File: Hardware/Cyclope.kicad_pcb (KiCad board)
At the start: 2 copper layers, 71 parts, among them J1 M20-9762042, J2 Motor_2, J3 Motor_1, J4 Camera_Right, J5 Camera_Left, J6 Motherboard_Right, J7 Motherboard_Left, J8 FTDI, M1 FS5113R, M2 FS5113R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

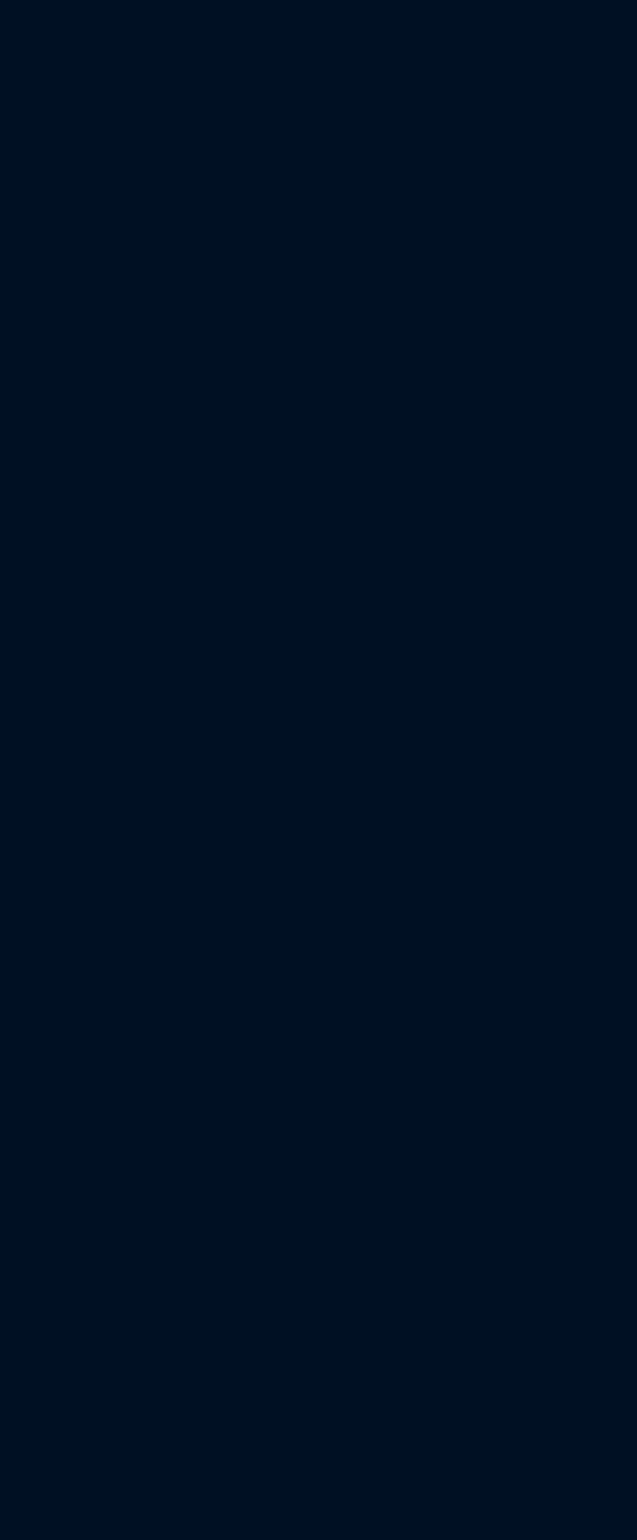
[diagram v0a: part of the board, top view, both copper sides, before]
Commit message: [Hardware] Added front board dimensions to PCB.
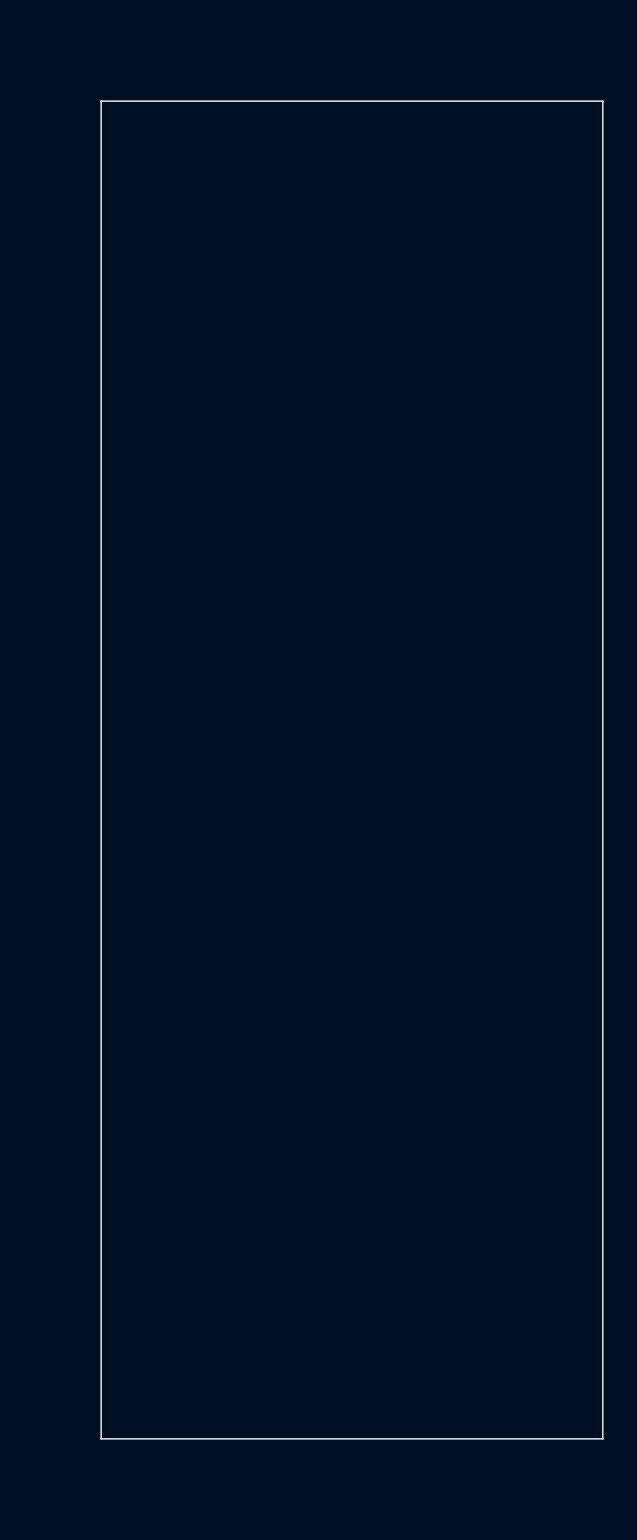
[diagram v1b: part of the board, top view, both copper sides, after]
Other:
- board outline added: 30 x 80 mm
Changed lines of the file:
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@@
   (general
     (thickness 1.6)
-    (drawings 1)
+    (drawings 8)
     (tracks 0)
     (zones 0)
@@
     )
   )
+  (dimension 25 (width 0.15) (layer Dwgs.User)
+    (gr_text "25,000 mm" (at 252.3 79.5 270) (layer Dwgs.User)
+      (effects (font (size 1 1) (thickness 0.15)))
+    )
+    (feature1 (pts (xy 240 92) (xy 251.586421 92)))
+    (feature2 (pts (xy 240 67) (xy 251.586421 67)))
+    (crossbar (pts (xy 251 67) (xy 251 92)))
+    (arrow1a (pts (xy 251 92) (xy 250.413579 90.873496)))
+    (arrow1b (pts (xy 251 92) (xy 251.586421 90.873496)))
+    (arrow2a (pts (xy 251 67) (xy 250.413579 68.126504)))
+    (arrow2b (pts (xy 251 67) (xy 251.586421 68.126504)))
+  )
+  (dimension 16 (width 0.15) (layer Dwgs.User)
+    (gr_text "16,000 mm" (at 252.3 48 270) (layer Dwgs.User)
+      (effects (font (size 1 1) (thickness 0.15)))
+    )
+    (feature1 (pts (xy 240 56) (xy 251.586421 56)))
+    (feature2 (pts (xy 240 40) (xy 251.586421 40)))
+    (crossbar (pts (xy 251 40) (xy 251 56)))
+    (arrow1a (pts (xy 251 56) (xy 250.413579 54.873496)))
+    (arrow1b (pts (xy 251 56) (xy 251.586421 54.873496)))
+    (arrow2a (pts (xy 251 40) (xy 250.413579 41.126504)))
+    (arrow2b (pts (xy 251 40) (xy 251.586421 41.126504)))
+  )
+  (dimension 16 (width 0.15) (layer Dwgs.User)
+    (gr_text "16,000 mm" (at 254.3 112 90) (layer Dwgs.User)
+      (effects (font (size 1 1) (thickness 0.15)))
+    )
+    (feature1 (pts (xy 240 104) (xy 253.586421 104)))
+    (feature2 (pts (xy 240 120) (xy 253.586421 120)))
+    (crossbar (pts (xy 253 120) (xy 253 104)))
+    (arrow1a (pts (xy 253 104) (xy 253.586421 105.126504)))
+    (arrow1b (pts (xy 253 104) (xy 252.413579 105.126504)))
+    (arrow2a (pts (xy 253 120) (xy 253.586421 118.873496)))
+    (arrow2b (pts (xy 253 120) (xy 252.413579 118.873496)))
+  )
+  (gr_line (start 240 40) (end 240 120) (layer Edge.Cuts) (width 0.1))
+  (gr_line (start 210 40) (end 240 40) (layer Edge.Cuts) (width 0.1))
+  (gr_line (start 210 120) (end 210 40) (layer Edge.Cuts) (width 0.1))
+  (gr_line (start 240 120) (end 210 120) (layer Edge.Cuts) (width 0.1))
   (gr_text GND (at 169.164 113.792) (layer F.Mask)
     (effects (font (size 1 1) (thickness 0.15)))

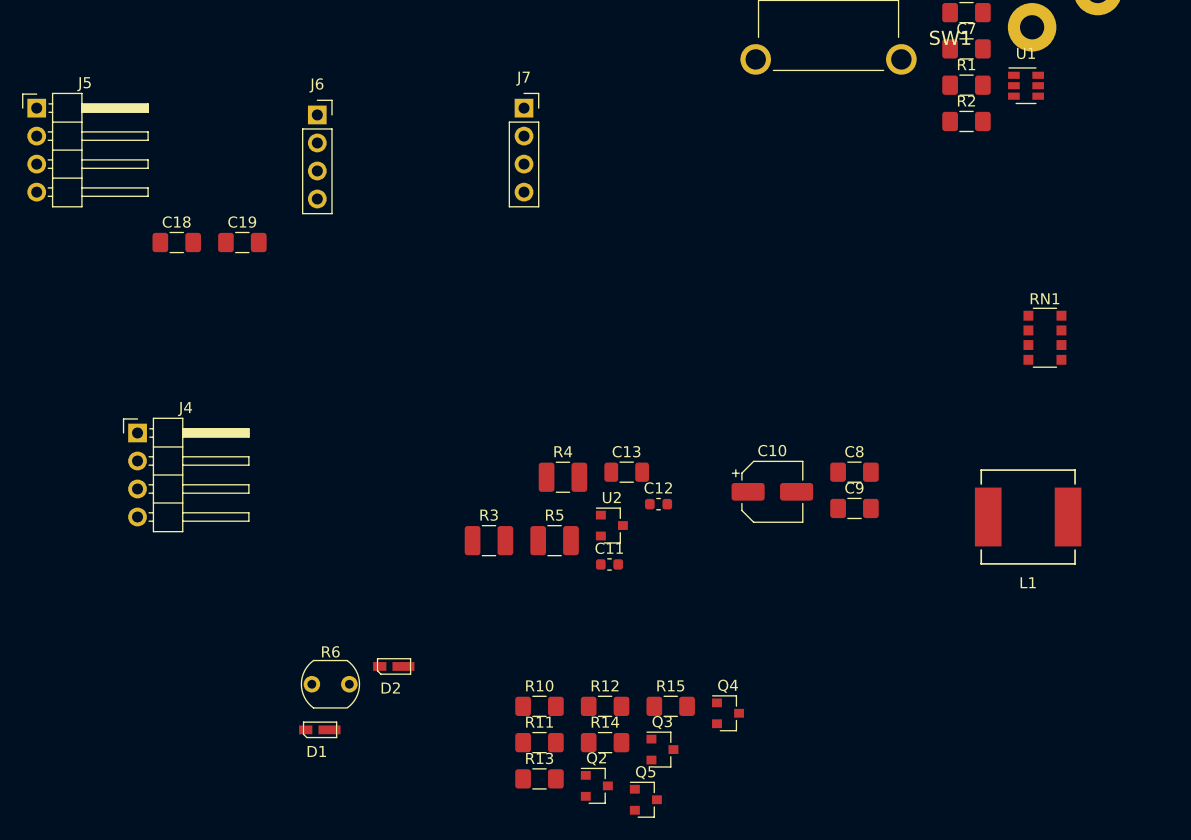
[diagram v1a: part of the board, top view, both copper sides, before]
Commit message: [Hardware] Added front board mounting holes.
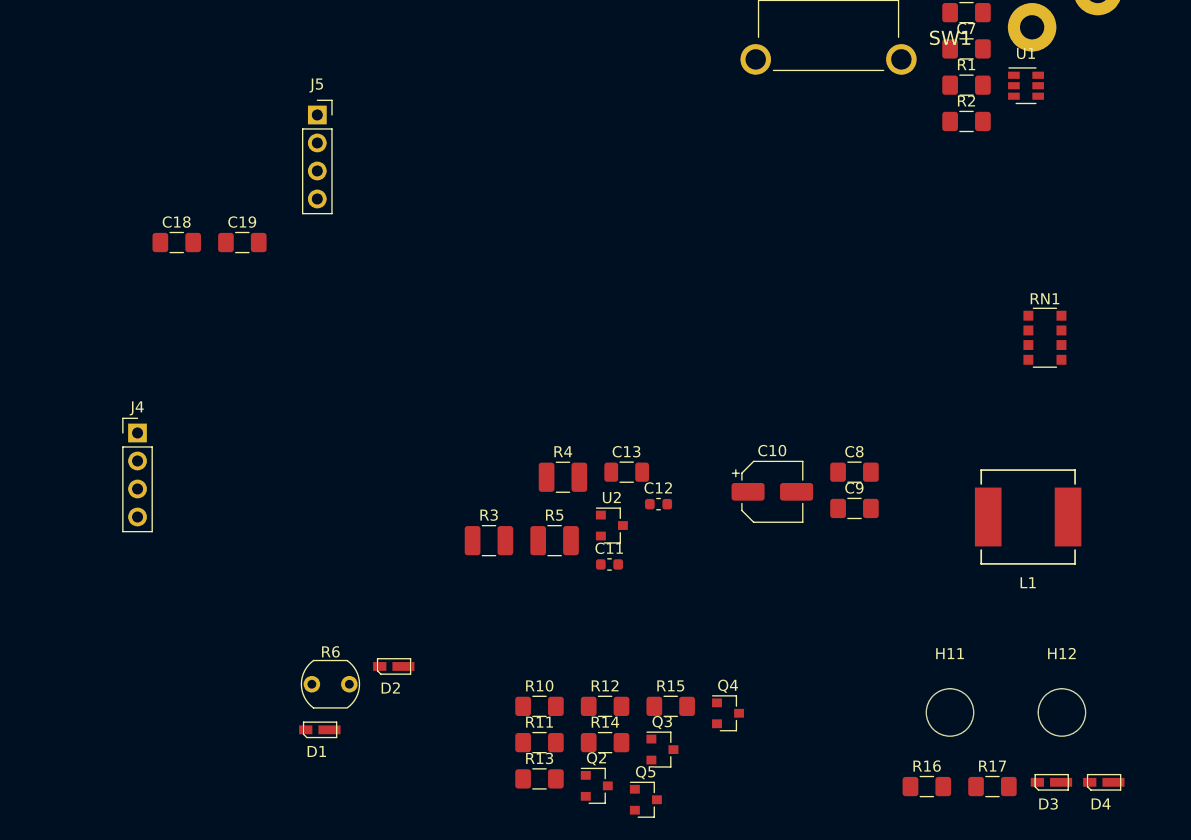
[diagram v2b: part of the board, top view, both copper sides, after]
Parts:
- removed the J5 at (47.2, 85.9)
- removed J7: Motherboard_Left, Connector_PinSocket_2.54mm:PinSocket_1x04_P2.54mm_Vertical
- added D3: 158301250, 158301250:158301250, F.Cu at (139.0, 147.0)
- added D4: 158301250, 158301250:158301250, F.Cu at (143.8, 147.0)
- added H11: Front_Board, MountingHole:MountingHole_4.3mm_M4, F.Cu at (130.1, 140.7)
- added H12: Front_Board, MountingHole:MountingHole_4.3mm_M4, F.Cu at (140.2, 140.7)
- added R16: 100, Resistor_SMD:R_1206_3216Metric_Pad1.42x1.75mm_HandSolder, F.Cu at (128.0, 147.4)
- added R17: 100, Resistor_SMD:R_1206_3216Metric_Pad1.42x1.75mm_HandSolder, F.Cu at (133.9, 147.4)
- J4: value Camera_Right -> Front; footprint Connector_PinHeader_2.54mm:PinHeader_1x04_P2.54mm_Horizontal -> Connector_PinHeader_2.54mm:PinHeader_1x04_P2.54mm_Vertical
- J5: renamed from J6; value Motherboard_Right -> Front
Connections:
- net CAMERA_BOARD_LEDS renamed FRONT_BOARD_LEDS
- J4 pad 2: +5VD -> Net-(J4-Pad2)
- J4 pad 3: +5VD -> Net-(D1-Pad1)
- J4 pad 4: Net-(J4-Pad4) -> GNDD
- J5 pad 1: CAMERA_BOARD_LDR -> GND
- J5 pad 2: +5V -> Net-(J5-Pad2)
- J5 pad 3: +5V -> FRONT_BOARD_LDR
- Q1 pad 3: Net-(J7-Pad4) -> Net-(J5-Pad2)
- R5 pad 2: CAMERA_BOARD_LDR -> FRONT_BOARD_LDR
- R6 pad 1: Net-(J4-Pad4) -> Net-(J4-Pad2)
- U3 pad 3: CAMERA_BOARD_LDR -> FRONT_BOARD_LDR

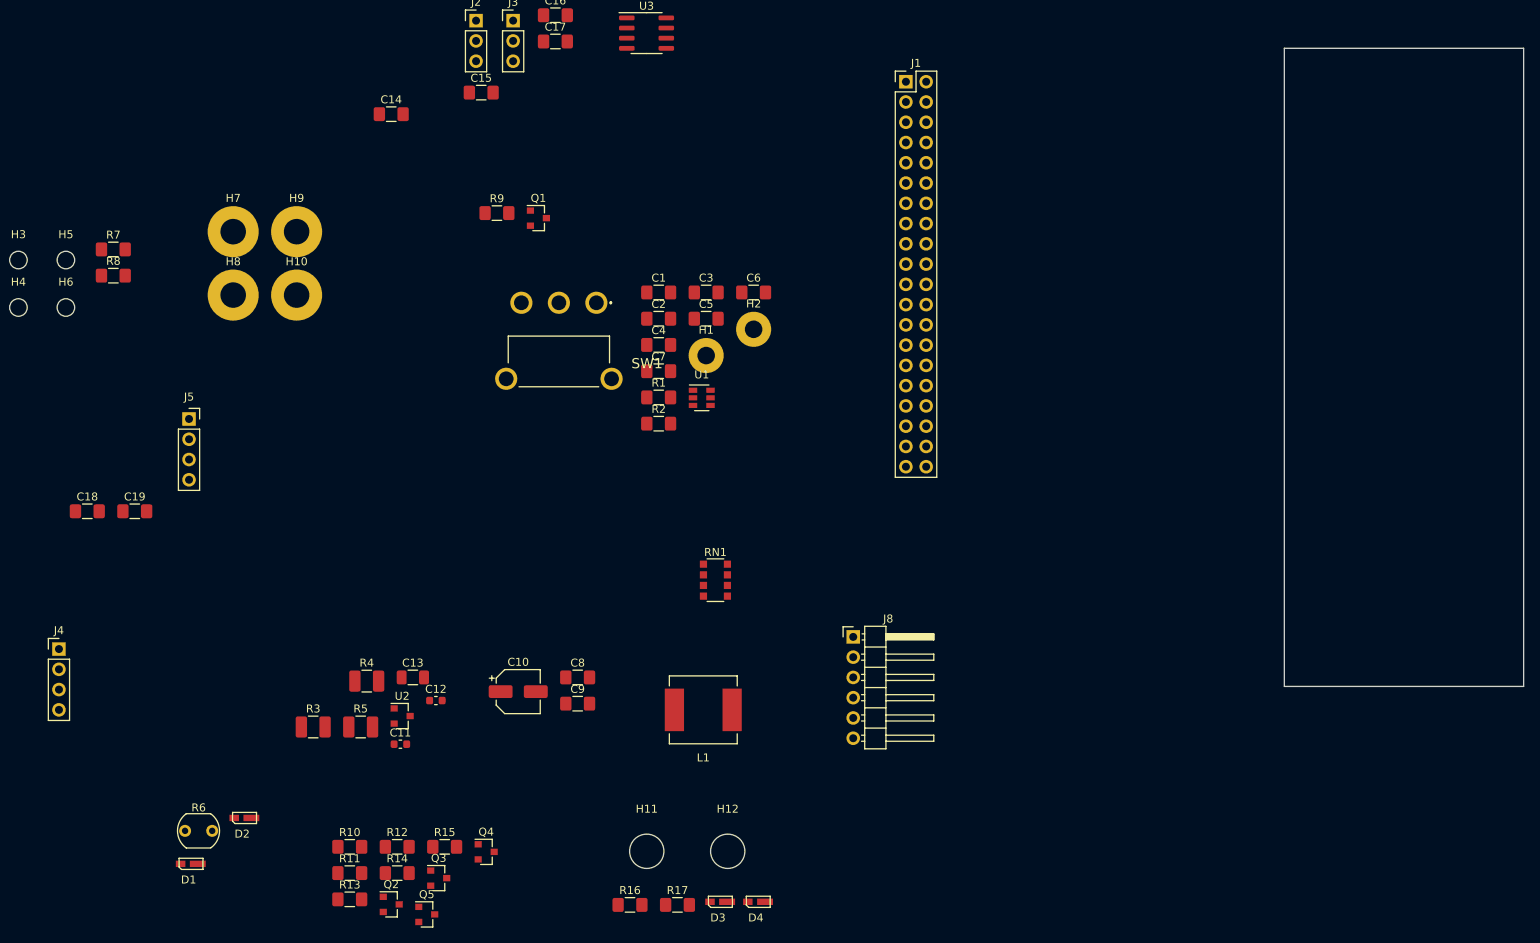
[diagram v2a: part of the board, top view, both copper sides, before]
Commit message: [Hardware] Added leds, connector and round corners to front board PCB.
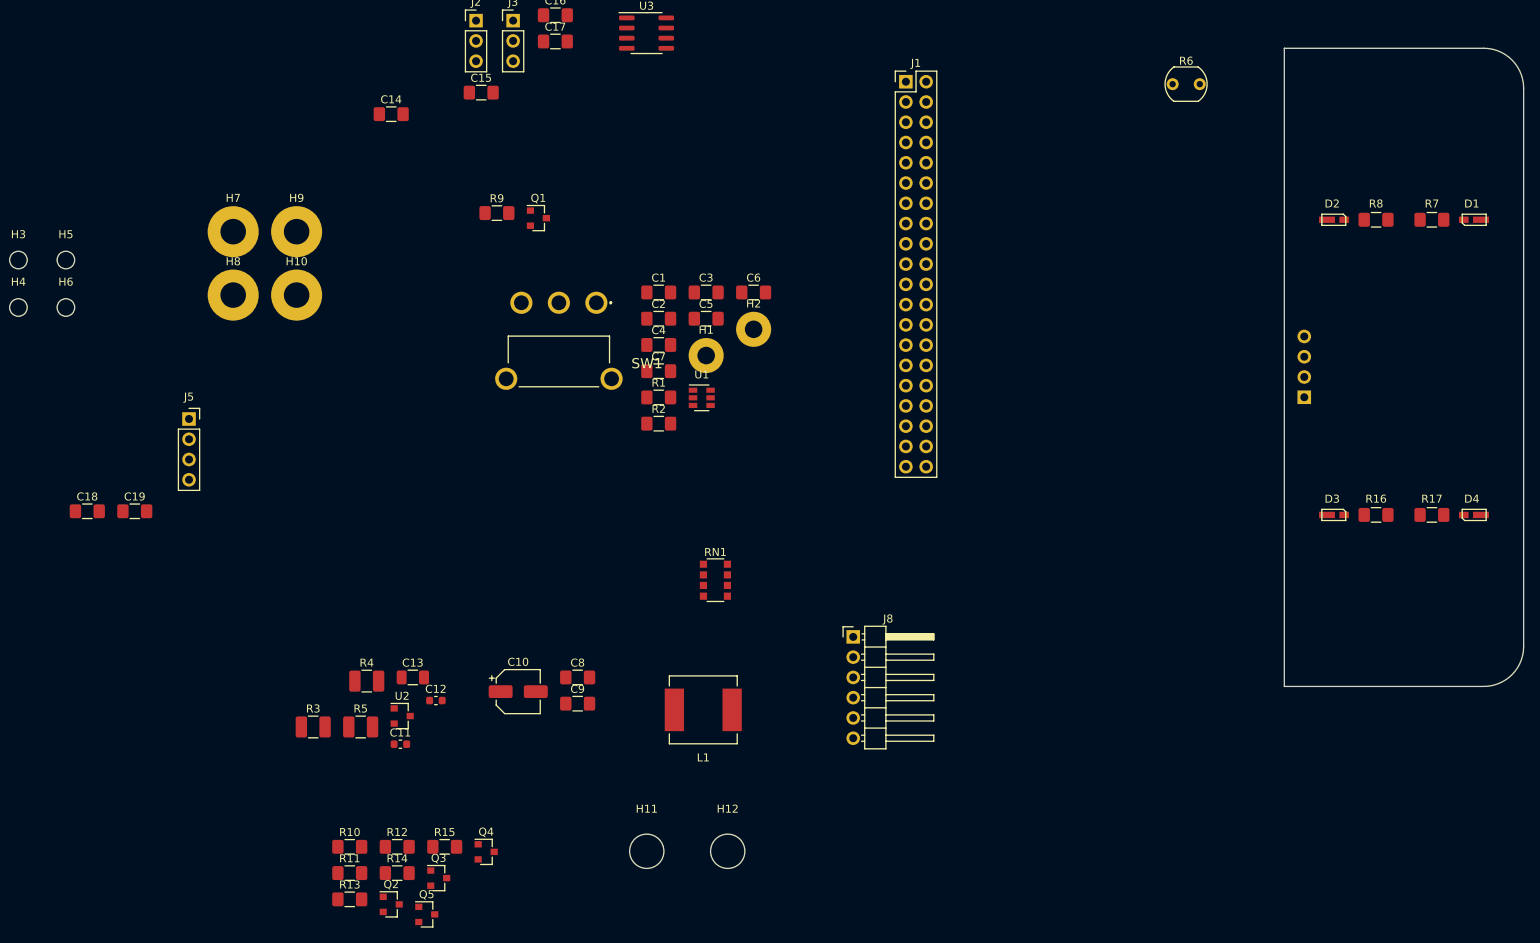
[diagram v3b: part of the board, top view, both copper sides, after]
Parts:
- J4: moved to B.Cu
- moved D1 180.0 mm to (233.5, 61.5)
- moved R7 165.3 mm to (228.5, 61.5)
- moved J4 159.3 mm to (212.5, 83.8)
- moved R8 158.4 mm to (221.5, 61.5), turned to 180 degrees
- moved D2 156.3 mm to (216.5, 61.5), turned to 180 degrees
- moved R6 155.2 mm to (196.0, 44.5)
- moved R17 106.5 mm to (228.5, 98.5)
- moved R16 105.5 mm to (221.5, 98.5), turned to 180 degrees
- moved D4 102.0 mm to (233.5, 98.5)
- moved D3 91.4 mm to (216.5, 98.5), turned to 180 degrees
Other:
- outline, holes or cut-outs redrawn
